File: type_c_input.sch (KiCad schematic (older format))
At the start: 32 parts, among them J15 USB_C_Receptacle_USB2.0, Q16 VBA2625, Q17 VBA2625, U11 STUSB4500

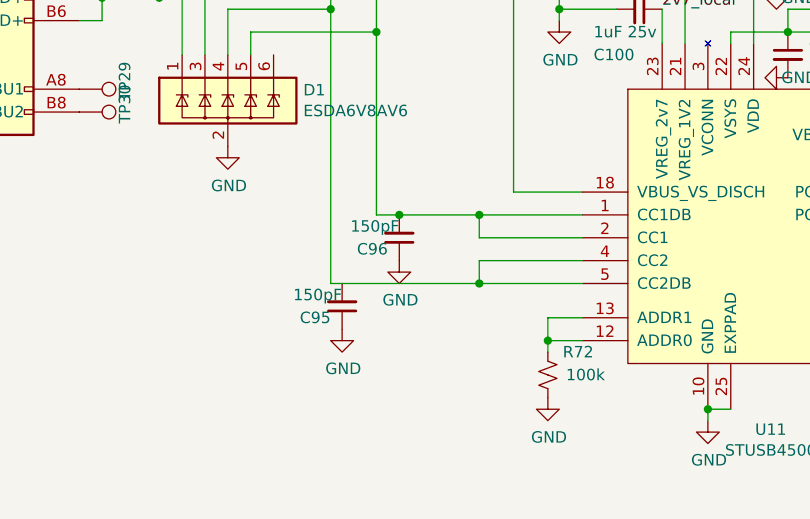
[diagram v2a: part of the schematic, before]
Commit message: Layout placed type-c + barrel jack
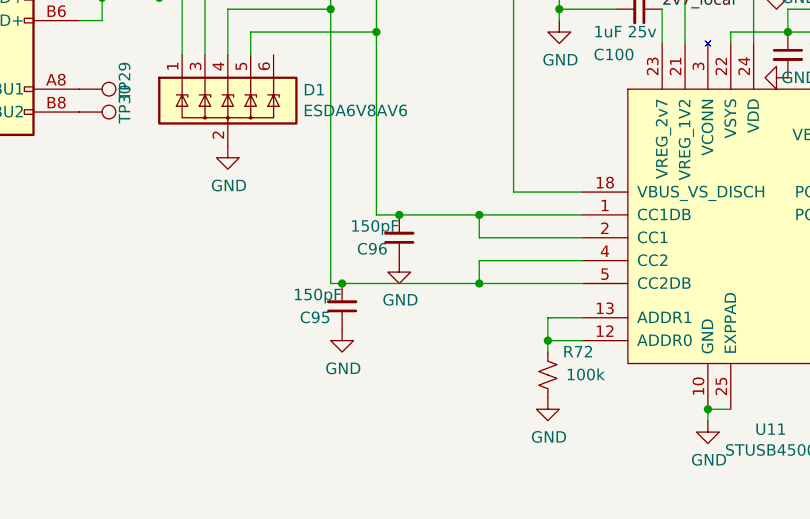
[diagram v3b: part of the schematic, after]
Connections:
- net at D1.4 (IO3), J15.B5 (CC2), U11.4 (CC2)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: now also C95.2
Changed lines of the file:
@@
 $Descr A4 11693 8268
 encoding utf-8
-Sheet 7 10
+Sheet 10 10
 Title ""
 Date ""
@@
 	3100 1800 3100 2250
 Wire Wire Line
-	3100 3450 3750 3450
+	3100 3450 3150 3450
 Wire Wire Line
 	4200 3350 3750 3350
@@
 	-1   0    0    1
 $EndComp
+Connection ~ 3150 3450
+Wire Wire Line
+	3150 3450 3750 3450
 $EndSCHEMATC

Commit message: Much layout wow.
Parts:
- removed R62, R63: 100k, lc_lib:0402_R, symbol Device:R_Small_US
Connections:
- net INPUT_TYPEC_VBUS_RAW: now reaches C101.1, C97.2, C98.1, D5.2 (A), J15.A4 (VBUS), J15.A9 (VBUS), J15.B4 (VBUS), J15.B9 (VBUS), Q16.5 (D), Q16.6 (D), Q16.7 (D), Q16.8 (D), R61.1, TP31.1, U11.24 (VDD)
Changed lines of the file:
@@
 	3900 1800 3900 1500
 Connection ~ 3900 1500
-Wire Wire Line
-	3900 1500 4750 1500
 $Comp
 L Device:C_Small C98
@@
 Wire Wire Line
 	6300 3150 6700 3150
-$Comp
-L Device:R_Small_US R?
-U 1 1 60088C40
-P 4750 1400
-AR Path="/5FD99B08/60088C40" Ref="R?"  Part="1"
-AR Path="/5FF1D194/60088C40" Ref="R?"  Part="1"
-AR Path="/5FF971C1/60088C40" Ref="R63"  Part="1"
-F 0 "R63" H 4500 1500 50  0000 L CNN
-F 1 "100k" H 4500 1400 50  0000 L CNN
-F 2 "lc_lib:0402_R" H 4750 1400 50  0001 C CNN
-F 3 "~" H 4750 1400 50  0001 C CNN
-F 4 "C25741" V 4750 1400 50  0001 C CNN "LCSC"
-	1    4750 1400
-	1    0    0    -1
-$EndComp
-Connection ~ 4750 1500
-Wire Wire Line
-	4750 1500 4950 1500
-$Comp
-L Device:R_Small_US R?
-U 1 1 6008A123
-P 4750 950
-AR Path="/5FD99B08/6008A123" Ref="R?"  Part="1"
-AR Path="/5FF1D194/6008A123" Ref="R?"  Part="1"
-AR Path="/5FF971C1/6008A123" Ref="R62"  Part="1"
-F 0 "R62" H 4550 850 50  0000 L CNN
-F 1 "100k" H 4500 950 50  0000 L CNN
-F 2 "lc_lib:0402_R" H 4750 950 50  0001 C CNN
-F 3 "~" H 4750 950 50  0001 C CNN
-F 4 "C25741" V 4750 950 50  0001 C CNN "LCSC"
-	1    4750 950
-	-1   0    0    1
-$EndComp
-Wire Wire Line
-	4750 1300 4750 1200
-$Comp
-L power:GND #PWR0184
-U 1 1 6008D6DA
-P 4750 850
-F 0 "#PWR0184" H 4750 600 50  0001 C CNN
-F 1 "GND" H 4755 677 50  0000 C CNN
-F 2 "" H 4750 850 50  0001 C CNN
-F 3 "" H 4750 850 50  0001 C CNN
-	1    4750 850
-	-1   0    0    1
-$EndComp
-Wire Wire Line
-	4750 1200 4850 1200
-Wire Wire Line
-	4850 1200 4850 1300
-Connection ~ 4750 1200
-Wire Wire Line
-	4750 1200 4750 1050
-Wire Wire Line
-	4850 1300 4900 1300
 Text HLabel 4900 1300 2    50   Input ~ 0
-INPUT_TYPEC_VBUS_DIV7
+INPUT_TYPEC_VBUS_RAW
 Text Label 6600 4100 0    50   ~ 0
 2v7_local
@@
 Wire Wire Line
 	3150 3450 3750 3450
+Wire Wire Line
+	3900 1500 4700 1500
+Wire Wire Line
+	4900 1300 4700 1300
+Wire Wire Line
+	4700 1300 4700 1500
+Connection ~ 4700 1500
+Wire Wire Line
+	4700 1500 4950 1500
 $EndSCHEMATC

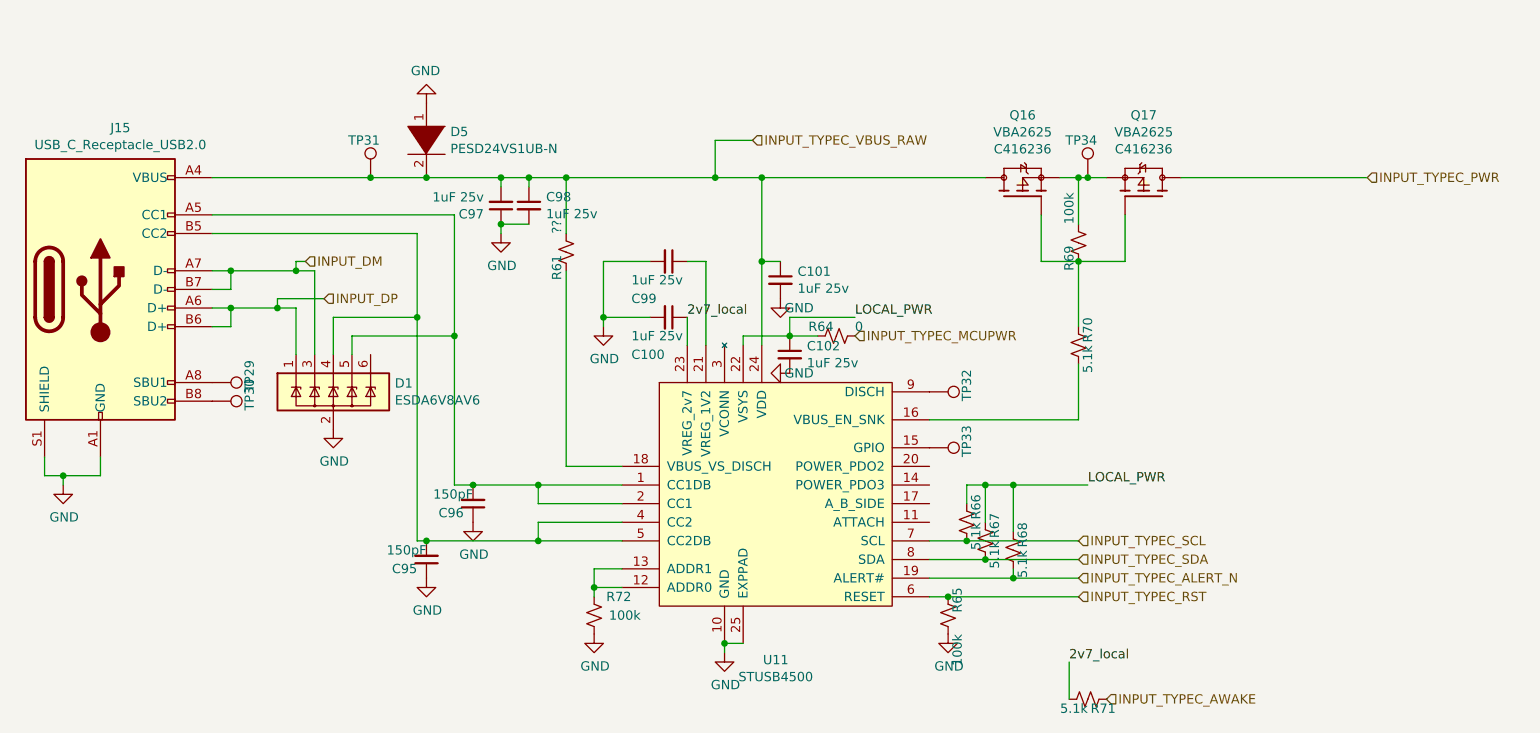
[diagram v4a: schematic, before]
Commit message: Almost connected MCU + ESP32 added leds addedd uart usb cleaned up type-c I/O -- STILL NEED TO level shift I2C
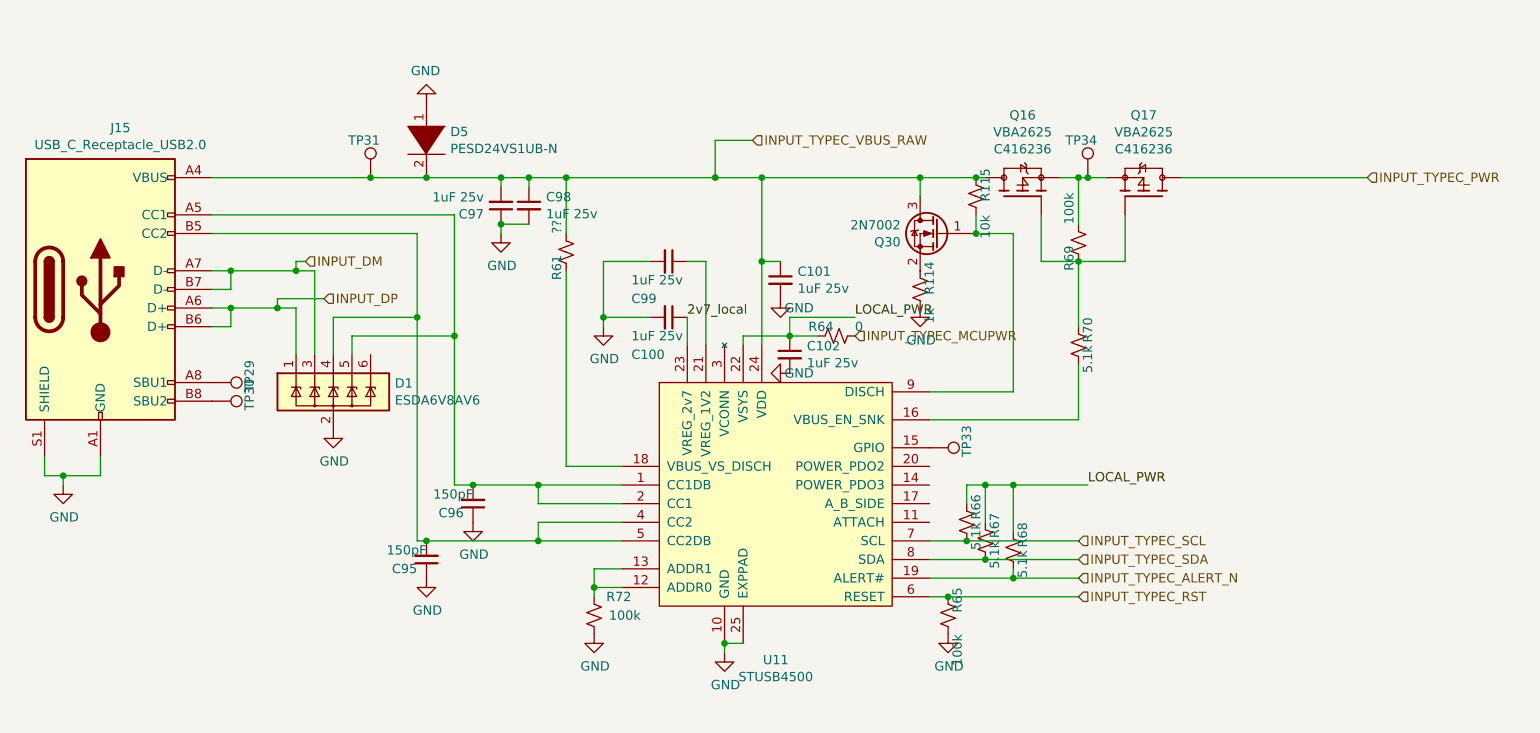
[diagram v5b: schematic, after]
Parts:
- removed R71: 5.1k, lc_lib:0402_R, symbol Device:R_Small_US
- removed TP32: TestPoint, TestPoint:TestPoint_Pad_D2.0mm, symbol Connector:TestPoint
- added Q30: 2N7002, Package_TO_SOT_SMD:SOT-23, symbol Device:Q_NMOS_GSD
- added R114: 1k, lc_lib:0402_R, symbol Device:R_Small_US
- added R115: 10k, lc_lib:0402_R, symbol Device:R_Small_US
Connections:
- net GND: now also R114.1
- net INPUT_TYPEC_VBUS_RAW: now also Q30.3 (D), R115.2
- net at U11.9 (DISCH): now also Q30.1 (G), R115.1
- new net: Q30.2 (S), R114.2
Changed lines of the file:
@@
 $EndComp
 Wire Wire Line
-	4950 1500 6150 1500
+	4950 1500 5800 1500
 Wire Wire Line
 	4200 3050 3900 3050
@@
 	-1   0    0    1
 $EndComp
-$Comp
-L Connector:TestPoint TP?
-U 1 1 600450A4
-P 5850 2650
-AR Path="/5FD15753/600450A4" Ref="TP?"  Part="1"
-AR Path="/5FD99B08/600450A4" Ref="TP?"  Part="1"
-AR Path="/5FF971C1/600450A4" Ref="TP32"  Part="1"
-F 0 "TP32" H 5900 2850 50  0000 R CNN
-F 1 "TestPoint" H 5300 2700 50  0001 R CNN
-F 2 "TestPoint:TestPoint_Pad_D2.0mm" H 6050 2650 50  0001 C CNN
-F 3 "~" H 6050 2650 50  0001 C CNN
-	1    5850 2650
-	0    1    1    0
-$EndComp
 Wire Wire Line
 	5850 2800 6650 2800
@@
 Text HLabel 4900 1300 2    50   Input ~ 0
 INPUT_TYPEC_VBUS_RAW
-Text Label 6600 4100 0    50   ~ 0
-2v7_local
-$Comp
-L Device:R_Small_US R?
-U 1 1 6009A960
-P 6700 4300
-AR Path="/5FD99B08/6009A960" Ref="R?"  Part="1"
-AR Path="/5FF1D194/6009A960" Ref="R?"  Part="1"
-AR Path="/5FF971C1/6009A960" Ref="R71"  Part="1"
-F 0 "R71" V 6650 4150 50  0000 L CNN
-F 1 "5.1k" V 6650 4300 50  0000 L CNN
-F 2 "lc_lib:0402_R" H 6700 4300 50  0001 C CNN
-F 3 "~" H 6700 4300 50  0001 C CNN
-F 4 "C25905" V 6700 4300 50  0001 C CNN "lcsc"
-	1    6700 4300
-	0    -1   -1   0
-$EndComp
-Wire Wire Line
-	6600 4300 6600 4100
-Text HLabel 6800 4300 2    50   Input ~ 0
-INPUT_TYPEC_AWAKE
 $Comp
 L Device:R_Small_US R?
@@
 Wire Wire Line
 	4700 1500 4950 1500
+$Comp
+L Device:Q_NMOS_GSD Q?
+U 1 1 60213422
+P 5900 1800
+AR Path="/5FD15753/60213422" Ref="Q?"  Part="1"
+AR Path="/600C8F88/60213422" Ref="Q?"  Part="1"
+AR Path="/5FF971C1/60213422" Ref="Q30"  Part="1"
+F 0 "Q30" H 6105 1754 50  0000 L CNN
+F 1 "2N7002" H 6105 1845 50  0000 L CNN
+F 2 "Package_TO_SOT_SMD:SOT-23" H 6100 1900 50  0001 C CNN
+F 3 "~" H 5900 1800 50  0001 C CNN
+F 4 "C8545" H 5900 1800 50  0001 C CNN "LCSC"
+	1    5900 1800
+	-1   0    0    -1
+$EndComp
+$Comp
+L Device:R_Small_US R?
+U 1 1 60213428
+P 5800 2100
+AR Path="/5FD99B08/60213428" Ref="R?"  Part="1"
+AR Path="/5FF1D194/60213428" Ref="R?"  Part="1"
+AR Path="/600C8F88/60213428" Ref="R?"  Part="1"
+AR Path="/5FF971C1/60213428" Ref="R114"  Part="1"
+F 0 "R114" V 5750 1950 50  0000 L CNN
+F 1 "1k" V 5750 2200 50  0000 L CNN
+F 2 "lc_lib:0402_R" H 5800 2100 50  0001 C CNN
+F 3 "~" H 5800 2100 50  0001 C CNN
+	1    5800 2100
+	-1   0    0    1
+$EndComp
+$Comp
+L Device:R_Small_US R?
+U 1 1 6021342E
+P 6100 1600
+AR Path="/5FD99B08/6021342E" Ref="R?"  Part="1"
+AR Path="/5FF1D194/6021342E" Ref="R?"  Part="1"
+AR Path="/600C8F88/6021342E" Ref="R?"  Part="1"
+AR Path="/5FF971C1/6021342E" Ref="R115"  Part="1"
+F 0 "R115" V 6050 1450 50  0000 L CNN
+F 1 "10k" V 6050 1700 50  0000 L CNN
+F 2 "lc_lib:0402_R" H 6100 1600 50  0001 C CNN
+F 3 "~" H 6100 1600 50  0001 C CNN
+	1    6100 1600
+	-1   0    0    1
+$EndComp
+Wire Wire Line
+	5800 1600 5800 1500
+Wire Wire Line
+	6100 1700 6100 1800
+$Comp
+L power:GND #PWR0255
+U 1 1 60213436
+P 5800 2200
+AR Path="/5FF971C1/60213436" Ref="#PWR0255"  Part="1"
+AR Path="/600C8F88/60213436" Ref="#PWR?"  Part="1"
+F 0 "#PWR0255" H 5800 1950 50  0001 C CNN
+F 1 "GND" H 5805 2027 50  0000 C CNN
+F 2 "" H 5800 2200 50  0001 C CNN
+F 3 "" H 5800 2200 50  0001 C CNN
+	1    5800 2200
+	1    0    0    -1
+$EndComp
+Wire Wire Line
+	6300 1800 6100 1800
+Connection ~ 6100 1800
+Connection ~ 5800 1500
+Wire Wire Line
+	5800 1500 6100 1500
+Connection ~ 6100 1500
+Wire Wire Line
+	6100 1500 6150 1500
+Wire Wire Line
+	5850 2650 6300 2650
+Wire Wire Line
+	6300 2650 6300 1800
 $EndSCHEMATC

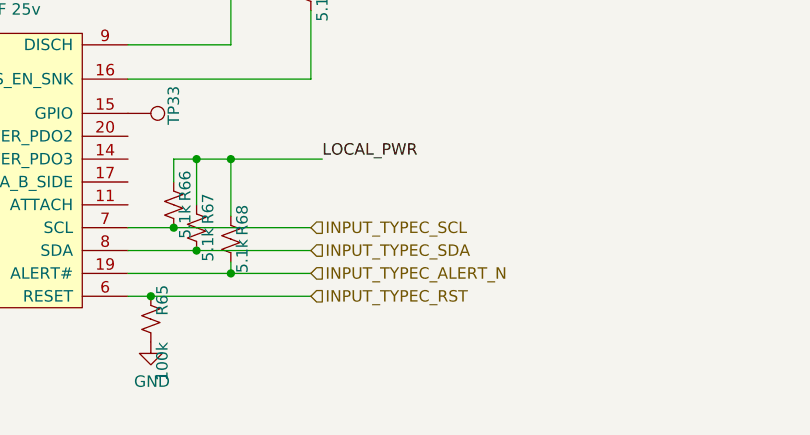
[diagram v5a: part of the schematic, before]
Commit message: lots of GPIO connectivity changes. fixed no PD on input fixed CH340G leakage. can otherwise power from GPIO. added fet for powering VCONN from 3v/5v NEED TO ADD OVERCURRENT
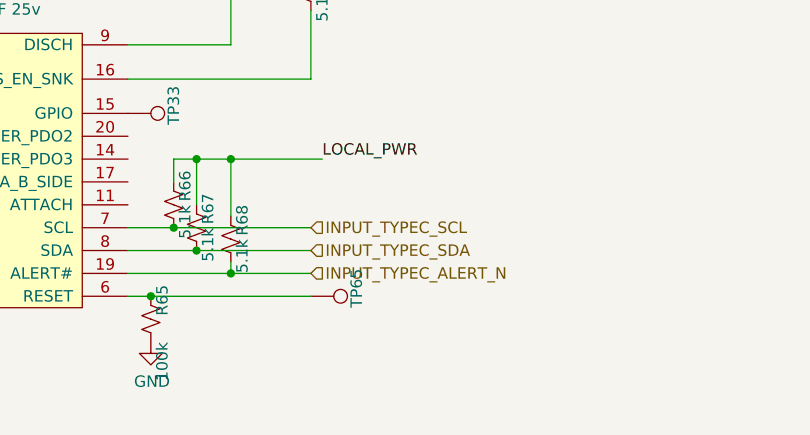
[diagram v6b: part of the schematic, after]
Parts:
- added TP65: TestPoint, TestPoint:TestPoint_Pad_D2.0mm, symbol Connector:TestPoint
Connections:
- net INPUT_TYPEC_RST: no longer names the net of R65.2, U11.6 (RESET)
- net INPUT_TYPEC_RST: now also TP65.1
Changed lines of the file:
@@
 	5950 3750 6650 3750
 Connection ~ 5950 3750
-Text HLabel 6650 3750 2    50   Input ~ 0
-INPUT_TYPEC_RST
 Text HLabel 6650 3550 2    50   Input ~ 0
 INPUT_TYPEC_SDA
@@
 Wire Wire Line
 	6300 2650 6300 1800
+$Comp
+L Connector:TestPoint TP?
+U 1 1 60264D92
+P 6650 3750
+AR Path="/5FD15753/60264D92" Ref="TP?"  Part="1"
+AR Path="/5FD99B08/60264D92" Ref="TP?"  Part="1"
+AR Path="/5FF971C1/60264D92" Ref="TP65"  Part="1"
+F 0 "TP65" H 6700 3950 50  0000 R CNN
+F 1 "TestPoint" H 6100 3800 50  0001 R CNN
+F 2 "TestPoint:TestPoint_Pad_D2.0mm" H 6850 3750 50  0001 C CNN
+F 3 "~" H 6850 3750 50  0001 C CNN
+	1    6650 3750
+	0    1    1    0
+$EndComp
 $EndSCHEMATC
